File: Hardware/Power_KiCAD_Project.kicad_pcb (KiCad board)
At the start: 4 copper layers, 80 x 93.2 mm, 83 parts, among them J1 Barrel_Jack_MountingPin, J2 XT60 Cell 5, J3 XT60 Cell 4, J4 XT60 Cell 3, J5 XT60 Cell 2, J6 XT60 Cell 1, J7 XT60 To External Switch, J8 L717SDC37P1ACH4F, Q1 PSMN2R6-40YS, Q2 BSS84PH6327XTSA2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

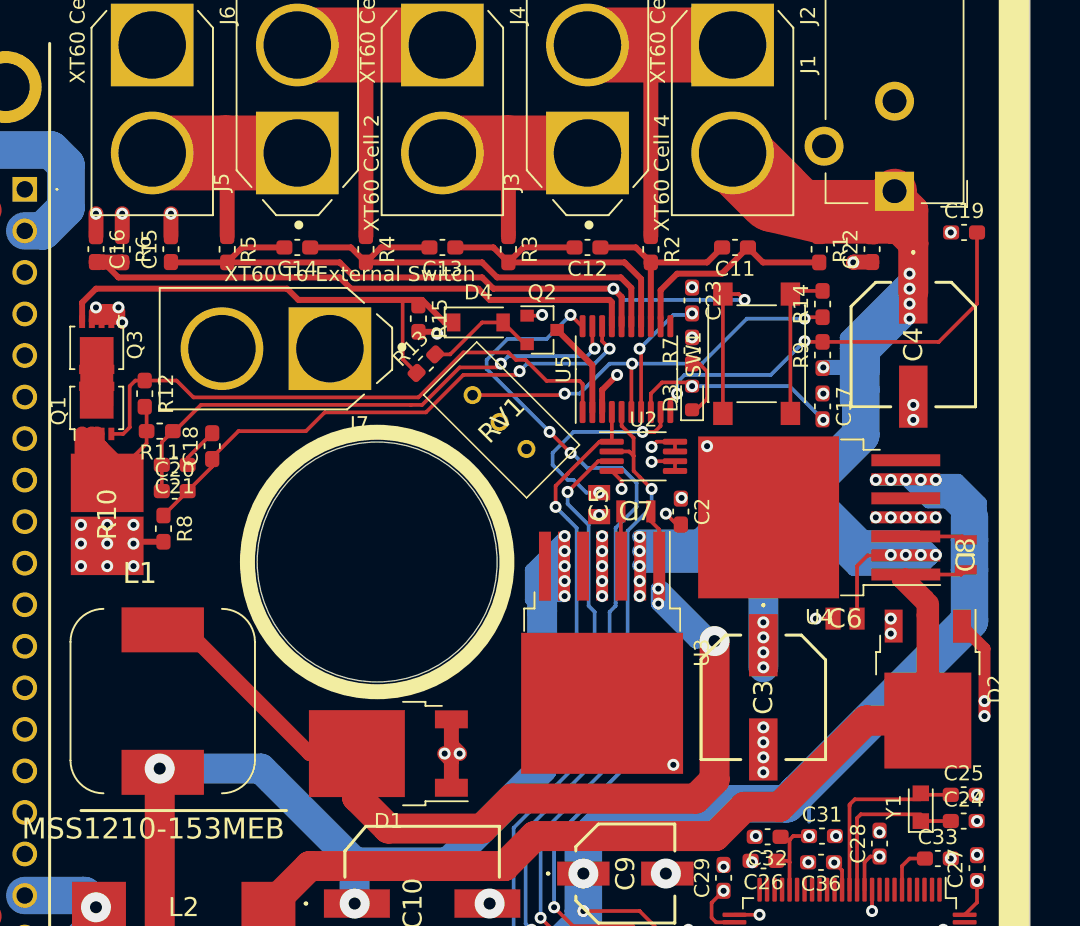
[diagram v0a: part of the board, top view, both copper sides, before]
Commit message: Completed all connections for GNDREF side of board
Having C18 and C21 connected to GNDREF feels weird because it's bypassing the connector for the external switch. Will check this later
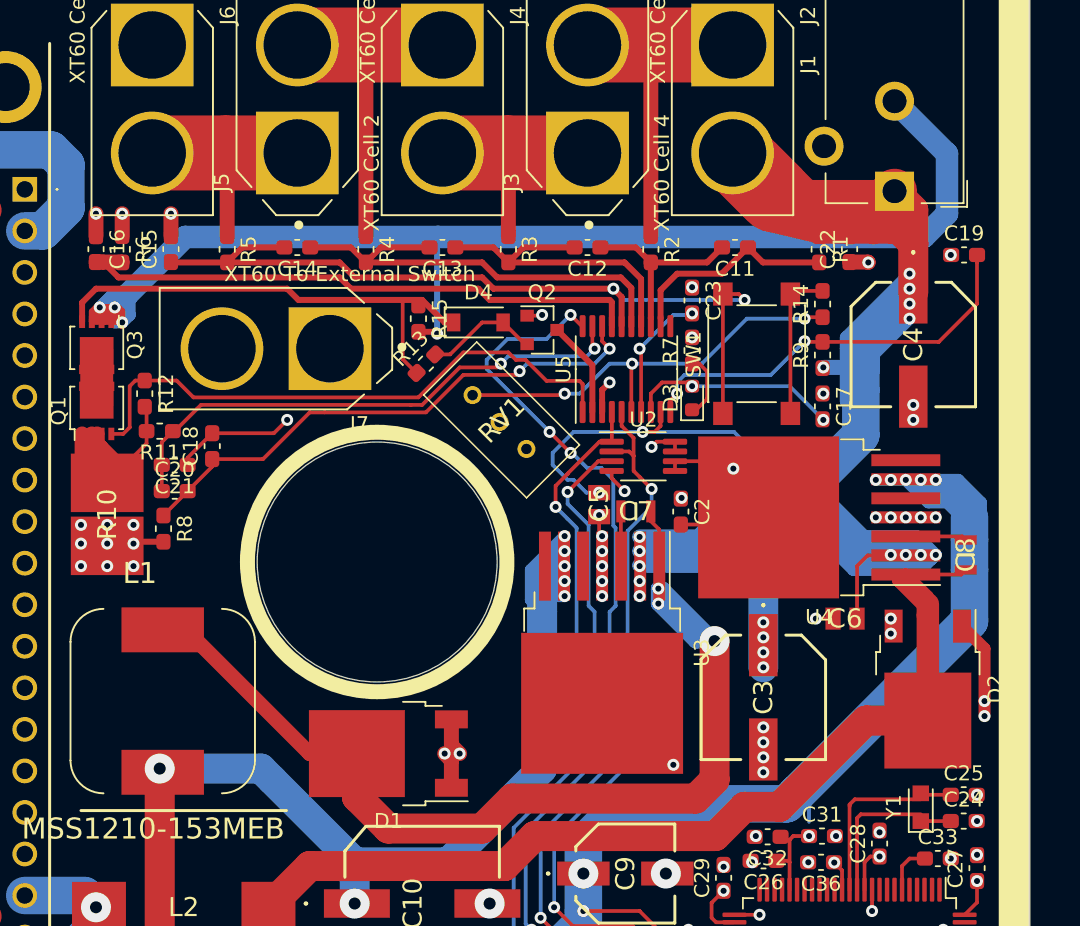
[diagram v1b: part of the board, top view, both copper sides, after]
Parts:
- moved C19 1.50 mm to (155.6, 78.0)
- moved C22 1.50 mm to (148.0, 77.6)
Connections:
- U4 pad 8: (no net) -> GND
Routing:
- net /LiPo Pack Monitor/PACK-: track 16.2 -> 97.2 mm
- net /PACK_M5: track 196.0 -> 207.5 mm
- net GND: track 30.5 -> 39.4 mm, vias 50 -> 49
- net GNDREF: track 13.3 -> 18.0 mm, vias 10 -> 11
- net /BATT_ALERT: track 69.2 -> 67.3 mm
- net Net-(C19-Pad2): track 29.5 -> 28.0 mm
- net (no net): vias 2 -> 1

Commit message: Routed data busses from MCU to DB37
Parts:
- moved R18 170.8 mm to (103.8, 130.6), turned to 90 degrees
- moved R19 170.7 mm to (99.5, 130.6), turned to 90 degrees
- moved D5 34.4 mm to (125.2, 128.8)
- moved R17 34.3 mm to (121.6, 130.5), turned to 180 degrees
- moved R16 32.4 mm to (121.6, 128.8), turned to 180 degrees
- moved D6 30.2 mm to (125.2, 130.5)
- moved C16 0.75 mm to (97.8, 78.4)
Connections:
- U4 pad 8: GND -> (no net)
- U6 pad 38: Net-(U6-Pad38) -> Net-(D5-Pad2)
- U6 pad 39: Net-(U6-Pad39) -> Net-(D6-Pad2)
- U6 pad 63: Net-(D6-Pad2) -> Net-(U6-Pad63)
- U6 pad 64: Net-(D5-Pad2) -> Net-(U6-Pad64)
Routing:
- net /DSUB-37_Bus/Alert_scl: track 0.00 -> 135.1 mm, vias 0 -> 3
- net /STM32L562VET6Q 1/DEBUG_SWDIO: track 0.00 -> 132.9 mm, vias 0 -> 2
- net /STM32L562VET6Q 1/DEBUG_SWCLK: track 0.00 -> 129.8 mm, vias 0 -> 2
- net /DSUB-37_Bus/Alert_sda: track 0.00 -> 129.3 mm, vias 0 -> 3
- net /DSUB-37_Bus/Alert_Active: track 0.00 -> 125.2 mm, vias 0 -> 2
- net /DSUB-37_Bus/NRST: track 2.05 -> 119.8 mm, vias 1 -> 4
- net Net-(D6-Pad2): track 0.00 -> 18.7 mm, vias 0 -> 2
- net Net-(D5-Pad2): track 0.00 -> 18.2 mm, vias 0 -> 2
- net +3V3: track 249.9 -> 259.3 mm, vias 18 -> 20
- net +5V: track 140.9 -> 146.9 mm
- net GND: track 39.4 -> 42.9 mm, vias 49 -> 51
- net Net-(D6-Pad1): track 0.00 -> 1.93 mm
- net Net-(D5-Pad1): track 0.00 -> 1.93 mm
- net /LiPo Pack Monitor/VC0: track 38.4 -> 37.8 mm

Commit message: All components and connections are made
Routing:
- net GND: track 42.9 -> 35.2 mm, vias 51 -> 52
- net +3V3: track 259.3 -> 259.5 mm, vias 20 -> 21
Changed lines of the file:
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@@
     (thickness 1.6)
     (drawings 27)
-    (tracks 948)
+    (tracks 951)
     (zones 0)
     (modules 83)
@@
     (34 B.Paste user)
     (35 F.Paste user)
-    (36 B.SilkS user)
+    (36 B.SilkS user hide)
     (37 F.SilkS user)
     (38 B.Mask user)
-    (39 F.Mask user)
+    (39 F.Mask user hide)
     (40 Dwgs.User user hide)
     (41 Cmts.User user)
@@
   (segment (start 137.6125 129.1125) (end 138 129.5) (width 0.25) (layer F.Cu) (net 2))
   (segment (start 137.225 129.1125) (end 137.6125 129.1125) (width 0.25) (layer F.Cu) (net 2))
-  (segment (start 142.124999 95.975001) (end 142.6 95.5) (width 0.25) (layer F.Cu) (net 2))
-  (segment (start 136.75 95.975001) (end 142.124999 95.975001) (width 0.25) (layer F.Cu) (net 2))
   (segment (start 131.3 96.55) (end 131.5 96.75) (width 0.25) (layer F.Cu) (net 2))
   (segment (start 131.3 95.35) (end 131.3 96.55) (width 0.25) (layer F.Cu) (net 2))
@@
   (segment (start 132.1375 92.8875) (end 133 93.75) (width 0.25) (layer F.Cu) (net 2))
   (segment (start 132.1375 92.405001) (end 132.1375 92.8875) (width 0.25) (layer F.Cu) (net 2))
-  (segment (start 139.244999 91.755001) (end 136.3625 91.755001) (width 0.25) (layer F.Cu) (net 2))
-  (segment (start 140.25 92.25) (end 139.244999 91.755001) (width 0.25) (layer F.Cu) (net 2))
-  (via (at 140.25 92.25) (size 0.8) (drill 0.4) (layers F.Cu B.Cu) (net 2))
   (segment (start 153.5 135.675) (end 153.5 134.25) (width 0.25) (layer F.Cu) (net 2))
   (via (at 152.75 133.5) (size 0.8) (drill 0.4) (layers F.Cu B.Cu) (net 2))
@@
   (via (at 119.5 130.5) (size 0.8) (drill 0.4) (layers F.Cu B.Cu) (net 2))
   (segment (start 120.749999 130.5) (end 119.5 130.5) (width 0.25) (layer F.Cu) (net 2))
+  (via (at 137.449998 92) (size 0.8) (drill 0.4) (layers F.Cu B.Cu) (net 2))
+  (segment (start 137.204999 91.755001) (end 137.449998 92) (width 0.25) (layer F.Cu) (net 2))
+  (segment (start 136.3625 91.755001) (end 137.204999 91.755001) (width 0.25) (layer F.Cu) (net 2))
+  (via (at 135.75 95.5) (size 0.8) (drill 0.4) (layers F.Cu B.Cu) (net 2))
+  (segment (start 136.225001 95.975001) (end 135.75 95.5) (width 0.25) (layer F.Cu) (net 2))
+  (segment (start 136.75 95.975001) (end 136.225001 95.975001) (width 0.25) (layer F.Cu) (net 2))
   (via (at 153.75 93) (size 0.8) (drill 0.4) (layers F.Cu B.Cu) (net 3))
   (via (at 152.75 93) (size 0.8) (drill 0.4) (layers F.Cu B.Cu) (net 3))
@@
   (segment (start 152 118.25) (end 151.5 118.75) (width 0.25) (layer F.Cu) (net 3))
   (segment (start 151.5 118.75) (end 151.5 120.325) (width 0.25) (layer F.Cu) (net 3))
-  (segment (start 153.025 118.25) (end 152 118.25) (width 0.25) (layer F.Cu) (net 3))
-  (segment (start 135.144999 90.455001) (end 134.8 90.8) (width 0.25) (layer F.Cu) (net 3))
-  (via (at 134.8 90.8) (size 0.8) (drill 0.4) (layers F.Cu B.Cu) (net 3))
-  (segment (start 136.3625 90.455001) (end 135.144999 90.455001) (width 0.25) (layer F.Cu) (net 3))
+  (segment (start 153.025 118.25) (end 153.025 118.25) (width 0.25) (layer F.Cu) (net 3))
   (segment (start 94.220002 76.395) (end 93 76.395) (width 2.5) (layer B.Cu) (net 3))
   (segment (start 95.75 74.865002) (end 94.220002 76.395) (width 2.5) (layer B.Cu) (net 3))
@@
   (segment (start 100.75 126) (end 105.25 126) (width 2.5) (layer B.Cu) (net 3))
   (segment (start 98.75 126) (end 100.75 126) (width 2.5) (layer B.Cu) (net 3))
+  (via (at 134.75 91.25) (size 0.8) (drill 0.4) (layers F.Cu B.Cu) (net 3))
+  (segment (start 135.544999 90.455001) (end 134.75 91.25) (width 0.25) (layer F.Cu) (net 3))
+  (segment (start 136.3625 90.455001) (end 135.544999 90.455001) (width 0.25) (layer F.Cu) (net 3))
+  (segment (start 153.025 118.25) (end 152 118.25) (width 0.25) (layer F.Cu) (net 3))
+  (via (at 153.025 118.25) (size 0.8) (drill 0.4) (layers F.Cu B.Cu) (net 3))
   (segment (start 150.25 74.5) (end 151 73.75) (width 3) (layer F.Cu) (net 4))
   (segment (start 145.979 74.521) (end 146 74.5) (width 1) (layer F.Cu) (net 4))
@@
     (connect_pads (clearance 1))
     (min_thickness 0.254)
-    (fill yes (arc_segments 32) (thermal_gap 0.508) (thermal_bridge_width 0.508) (smoothing fillet) (radius 2))
+    (fill yes (arc_segments 32) (thermal_gap 0.508) (thermal_bridge_width 0.508) (smoothing fillet) (radius 1.5))
     (polygon
       (pts

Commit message: Fixed issues with copper fill clearances
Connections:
- U3 pad 8: (no net) -> GND
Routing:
- net GND: vias 52 -> 53
- net (no net): vias 1 -> 0
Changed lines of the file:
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@@
     (pad "" smd rect (at 0.95 -2.775 270) (size 4.55 5.25) (layers F.Paste))
     (pad "" smd rect (at 5.8 2.775 270) (size 4.55 5.25) (layers F.Paste))
-    (pad 8 smd rect (at 3.375 0 270) (size 9.4 10.8) (layers F.Cu F.Mask))
+    (pad 8 smd rect (at 3.375 0 270) (size 9.4 10.8) (layers F.Cu F.Mask)
+      (net 2 GND))
     (pad 7 smd rect (at -5.775 3.81 270) (size 4.6 0.8) (layers F.Cu F.Paste F.Mask)
       (net 77 "Net-(U3-Pad7)"))
@@
   (via (at 151.75 98) (size 0.8) (drill 0.4) (layers F.Cu B.Cu) (net 4))
   (via (at 150.75 98) (size 0.8) (drill 0.4) (layers F.Cu B.Cu) (net 4))
-  (via (at 136.25 112) (size 0.8) (drill 0.4) (layers F.Cu B.Cu) (net 0))
+  (via (at 136.25 112) (size 0.8) (drill 0.4) (layers F.Cu B.Cu) (net 2))
   (segment (start 88.74 75.01) (end 90.46 75.01) (width 2) (layer F.Cu) (net 1))
   (segment (start 84.74 75.01) (end 88.74 75.01) (width 2) (layer F.Cu) (net 1))
@@
     (polygon
       (pts
-        (xy 109 95.75) (xy 108.5 99.75) (xy 95.75 99.75) (xy 95.75 85) (xy 102.5 85)
-        (xy 102.5 80.75) (xy 109 80.75)
+        (xy 108.5 95.75) (xy 108.5 99.25) (xy 96.25 99.25) (xy 96.25 85) (xy 103 85)
+        (xy 103 81.25) (xy 108.5 81.25)
       )
     )
@@
     (polygon
       (pts
-        (xy 157 87) (xy 148 87) (xy 148 89) (xy 125.75 89) (xy 125.75 90.5)
-        (xy 115.5 90.5) (xy 109.75 93.25) (xy 109.75 80) (xy 101.75 80) (xy 101.75 83.5)
-        (xy 95.75 83.5) (xy 95.75 59.25) (xy 157 59.25)
+        (xy 157 86.5) (xy 147.5 86.5) (xy 147.5 88.5) (xy 125.25 88.5) (xy 125.25 90)
+        (xy 115.75 90) (xy 110.25 93.375) (xy 110.25 80.125) (xy 101.25 80) (xy 101.25 83)
+        (xy 96.25 83) (xy 96.25 59.25) (xy 157 59.25)
       )
     )
@@
         (xy 111.5 104.75) (xy 113.25 105.75) (xy 116 106.5) (xy 119.25 106) (xy 121.75 104.5)
         (xy 123.25 102.75) (xy 124 101.25) (xy 124.5 98.75) (xy 124.25 96.5) (xy 122.75 93.5)
-        (xy 120 91.25) (xy 126.5 91.25) (xy 126.5 89.75) (xy 148.75 89.75) (xy 148.75 87.75)
+        (xy 120.75 91.75) (xy 127 91.75) (xy 127 89.75) (xy 148.75 89.75) (xy 148.75 87.75)
         (xy 157.25 87.75)
       )

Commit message: Adjusted silk screen labels
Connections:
- U3 pad 8: GND -> (no net)
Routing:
- net GND: vias 53 -> 52

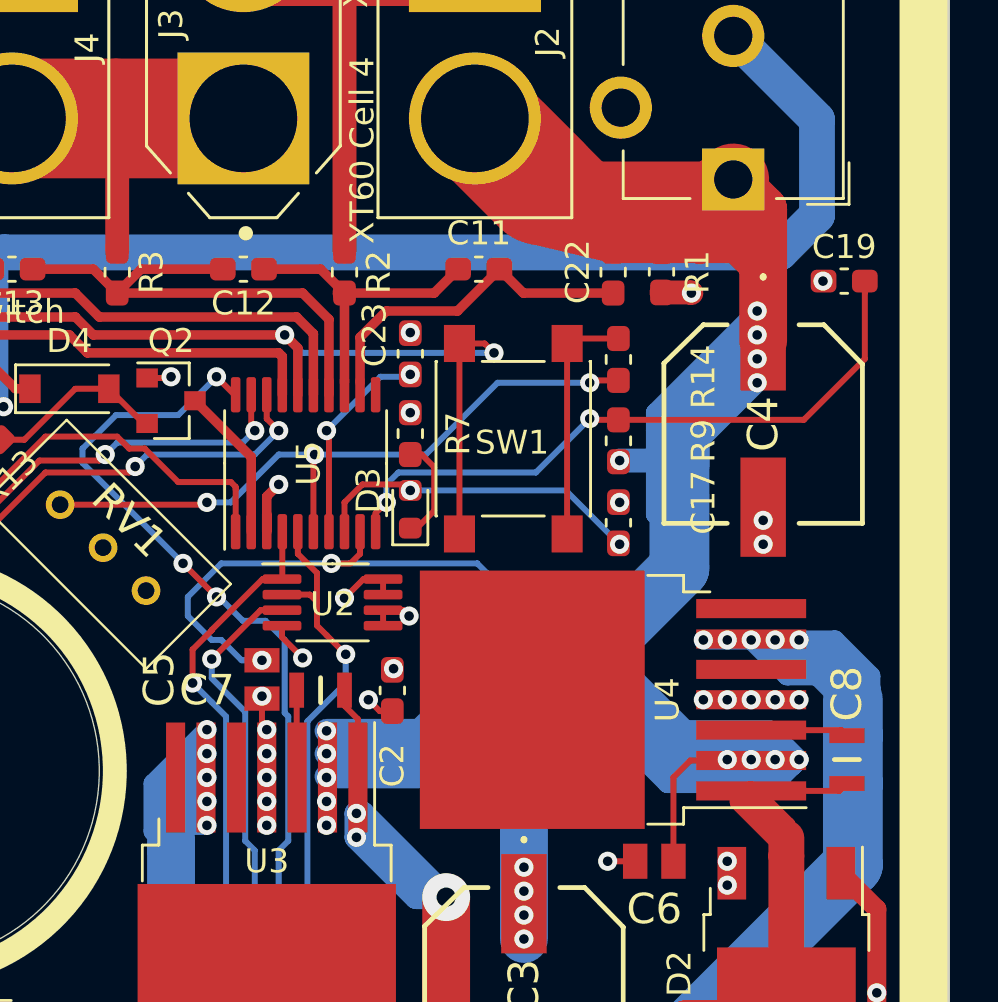
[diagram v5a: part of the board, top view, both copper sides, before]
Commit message: Adjusted power trace geometries
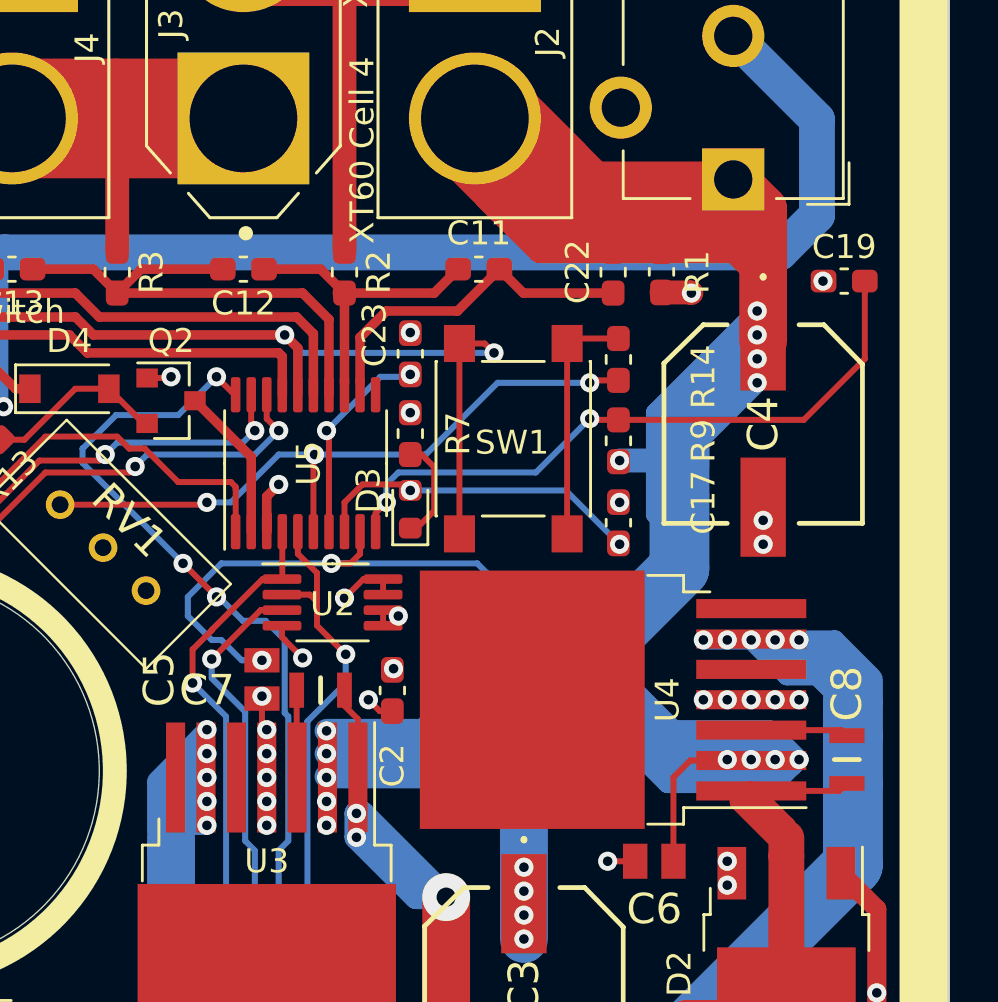
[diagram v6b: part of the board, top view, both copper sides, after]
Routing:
- net +3V3: track 259.5 -> 254.7 mm
- net +5V: track 146.9 -> 145.7 mm
- net /PACK_M5: track 207.5 -> 206.6 mm

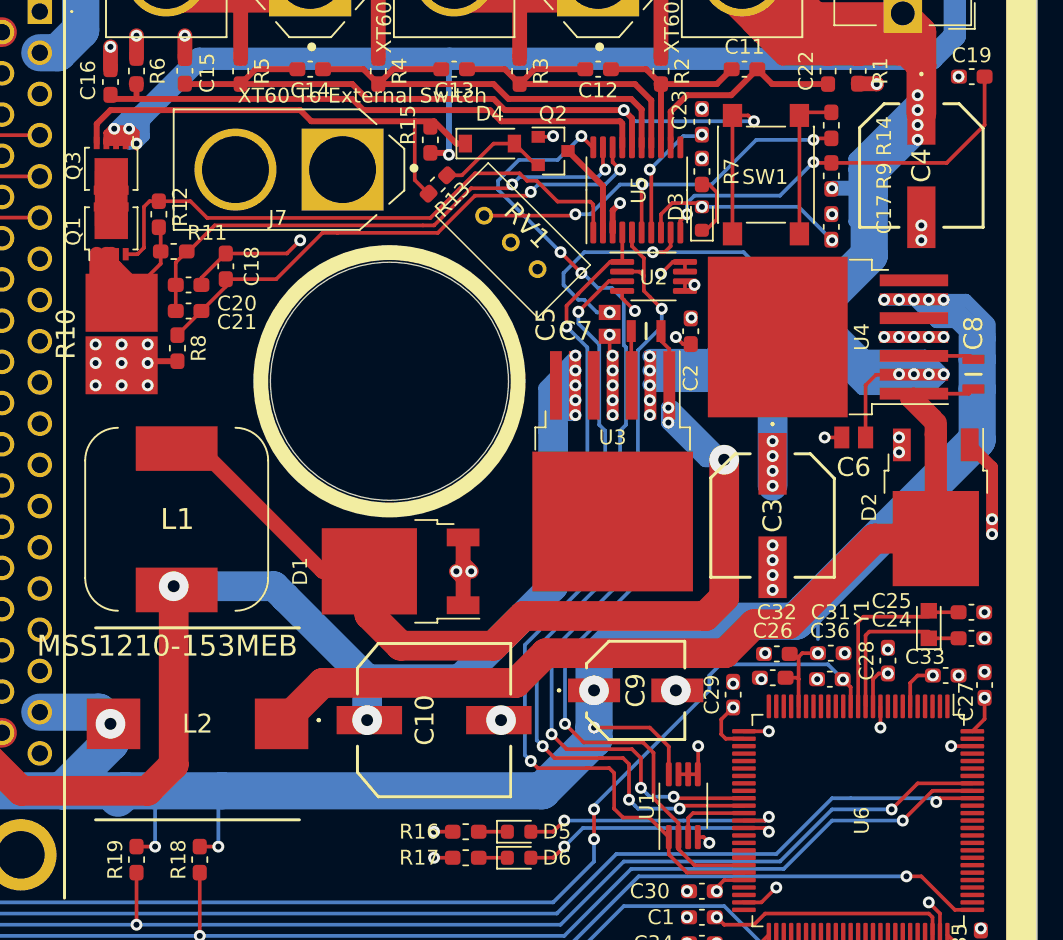
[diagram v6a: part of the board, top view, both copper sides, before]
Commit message: Adjusted position of vias to maximize clearance
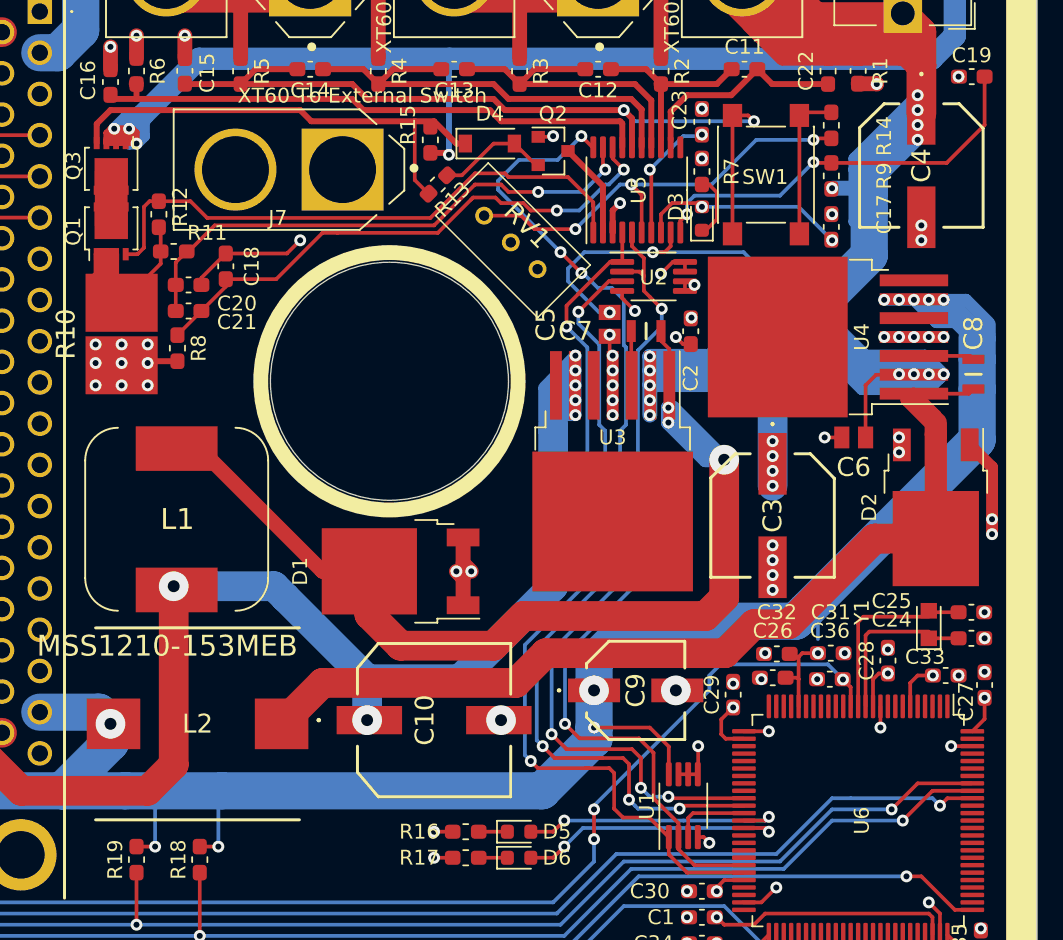
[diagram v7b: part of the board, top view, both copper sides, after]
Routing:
- net /PACK_M5: track 206.6 -> 213.0 mm
- net Net-(Q1-Pad1): track 25.3 -> 19.3 mm
- net +5V: track 145.7 -> 149.7 mm
- net /LiPo Pack Monitor/PACK-: track 97.2 -> 95.9 mm
- net Net-(R14-Pad1): track 28.7 -> 29.8 mm
- net Net-(C18-Pad1): track 36.9 -> 37.7 mm
- net +3V3: track 254.7 -> 254.0 mm
